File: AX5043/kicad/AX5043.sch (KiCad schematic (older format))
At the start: 29 parts, among them U1 AX5043, X1 12.000MHz, X2 SMA

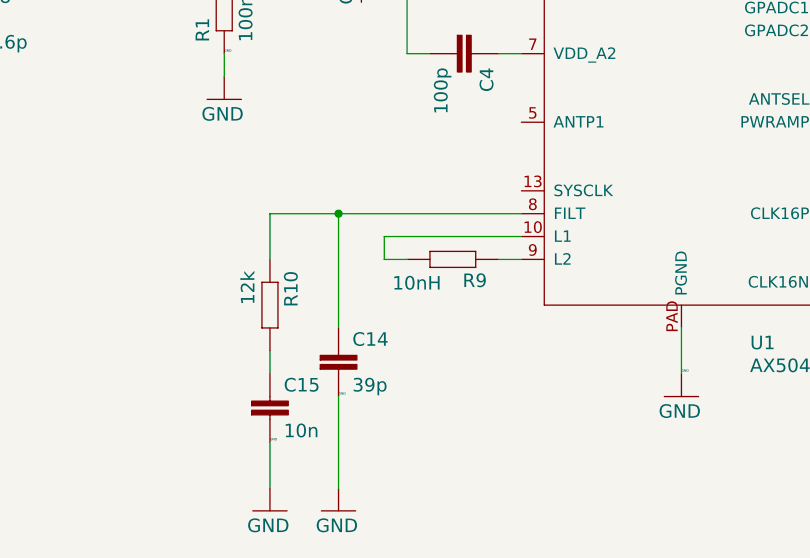
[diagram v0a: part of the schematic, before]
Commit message: Changed value of VCO coil inductor from 10nH to 6.8nH. Added BOM.
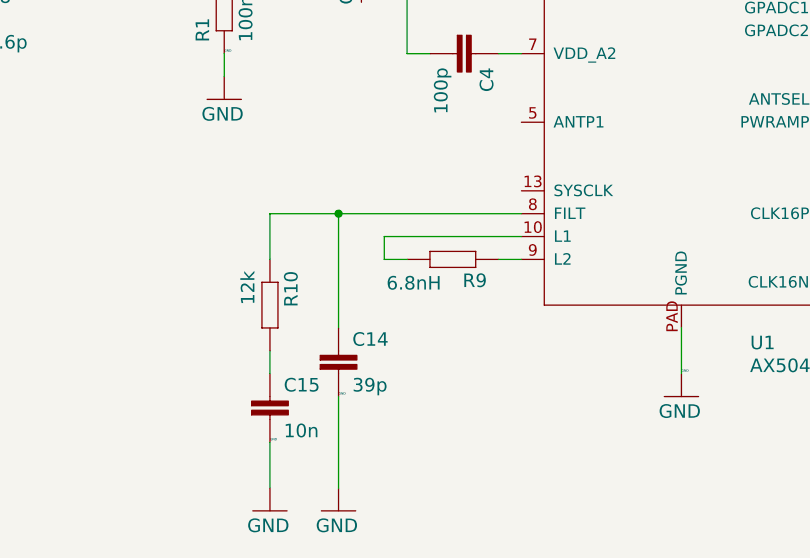
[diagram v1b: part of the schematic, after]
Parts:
- R9: value 10nH -> 6.8nH
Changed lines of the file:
@@
 P 4625 5800
 F 0 "R9" H 4475 5859 59  0000 L BNN
-F 1 "10nH" H 4675 5870 59  0000 L BNN
+F 1 "6.8nH" H 4675 5870 59  0000 L BNN
 F 2 "AX5043:R0603" H 4625 5800 50  0001 C CNN
 F 3 "" H 4625 5800 50  0001 C CNN
